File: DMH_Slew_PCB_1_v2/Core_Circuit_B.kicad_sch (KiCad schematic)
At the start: 52 parts, among them J6 TS_Jack_6.35mm_Sw, J60 Conn_01x08_PinHeader, J61 Conn_01x08_PinHeader, J7 TS_Jack_6.35mm_Sw, J8 TS_Jack_6.35mm_Sw, Q10 BC558, Q7 BC548, Q8 BC548, Q9 BC558, SW4 SW_DPDT_3way, SW5 SW_DPDT, SW6 SPDT_OnOffOn, U3 TL074, U4 TL074

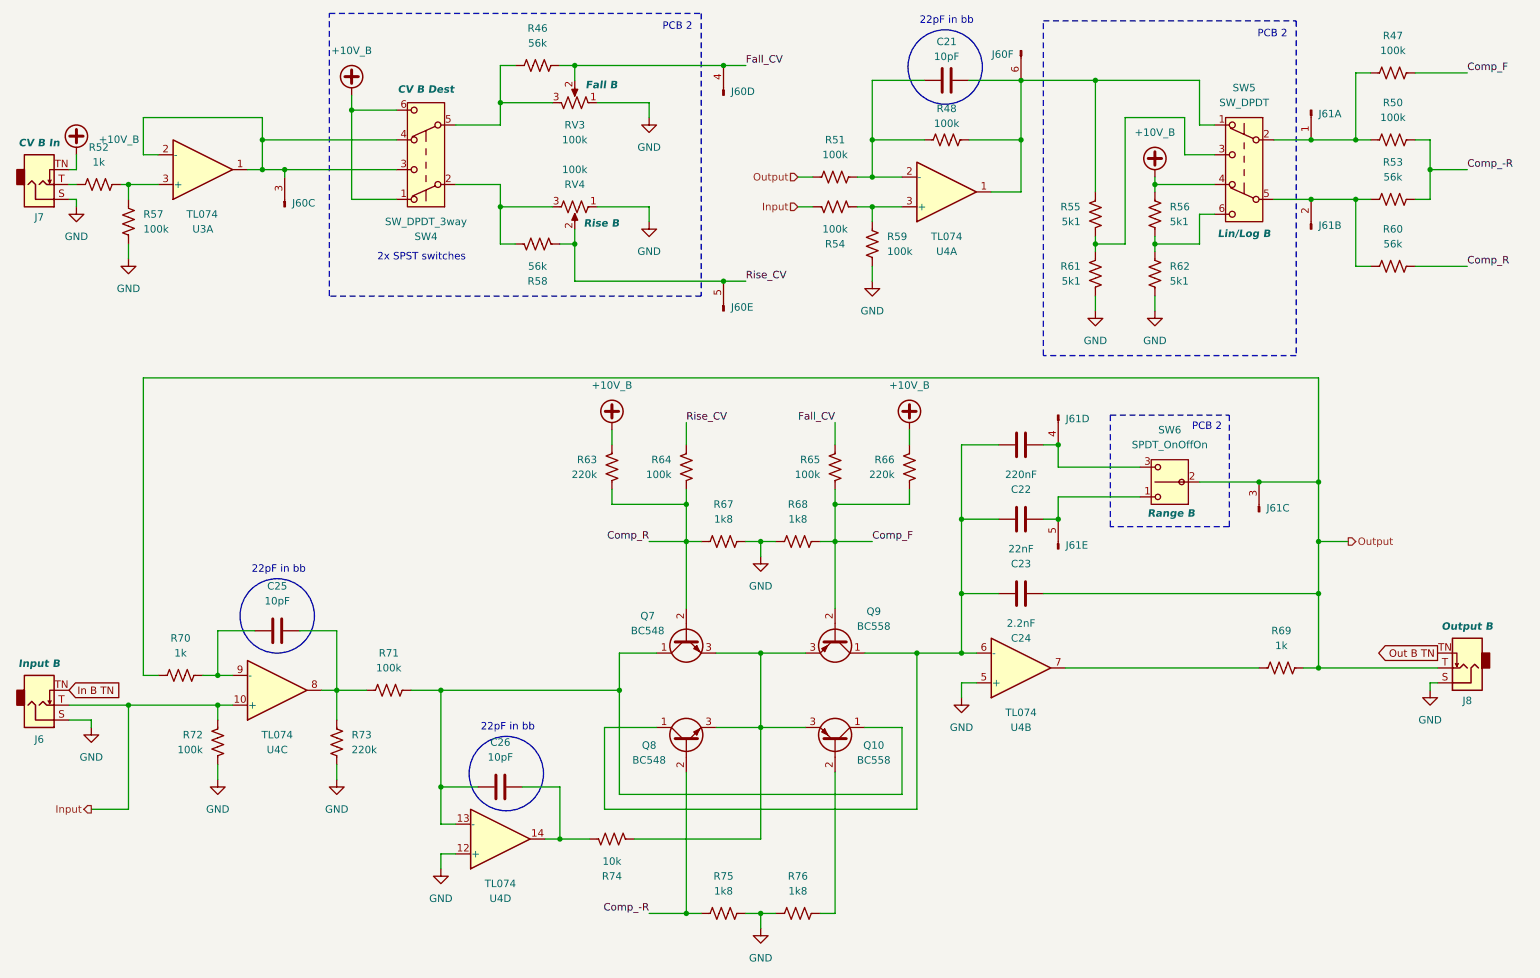
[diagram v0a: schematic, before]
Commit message: PCB 2 component placement done
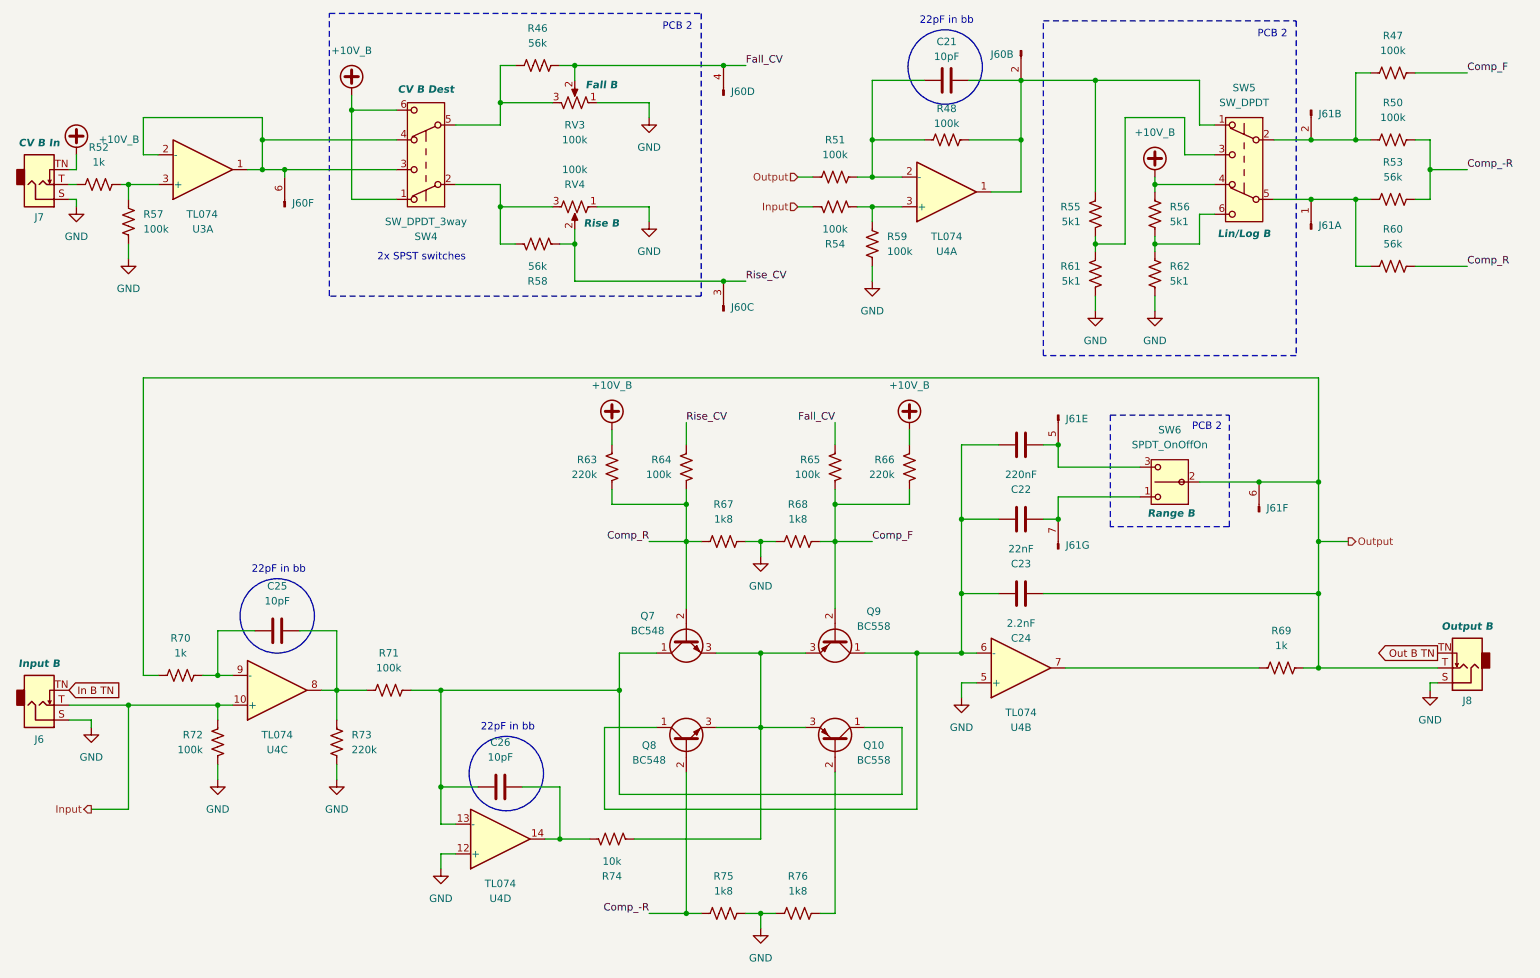
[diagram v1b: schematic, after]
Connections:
- net Output: now also J61.6 (Pin_6); no longer J61.3 (Pin_3)
- net Rise_CV: now also J60.3 (Pin_3); no longer J60.5 (Pin_5)
- net at C21.2, R48.1, R55.1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: now also J60.2 (Pin_2); no longer J60.6 (Pin_6)
- net at C22.2, SW6.3 (C): now also J61.5 (Pin_5); no longer J61.4 (Pin_4)
- net at R53.2, R60.2, SW5.5 (B): now also J61.1 (Pin_1); no longer J61.2 (Pin_2)
- net at SW4.3 (C), SW4.4 (A), U3.1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: now also J60.6 (Pin_6); no longer J60.3 (Pin_3)
- net at R47.2, R50.2, SW5.2 (B): now also J61.2 (Pin_2); no longer J61.1 (Pin_1)
- net at C23.2, SW6.1 (A): now also J61.7 (Pin_7); no longer J61.5 (Pin_5)
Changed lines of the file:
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@@
 		(at 190.5 30.48 90)
 		(mirror x)
-		(unit 6)
+		(unit 2)
 		(exclude_from_sim no)
 		(in_bom yes)
@@
 				(path "/58f4306d-5387-4983-bb08-41a2313fd315/77d402a4-d1d6-4e9c-af86-3ca5793147b8"
 					(reference "J60")
-					(unit 6)
+					(unit 2)
 				)
 			)
@@
 		(lib_id "SynthStuff:Conn_01x08_PinHeader")
 		(at 240.03 60.96 90)
-		(unit 2)
+		(unit 1)
 		(exclude_from_sim no)
 		(in_bom yes)
@@
 				(path "/58f4306d-5387-4983-bb08-41a2313fd315/77d402a4-d1d6-4e9c-af86-3ca5793147b8"
 					(reference "J61")
-					(unit 2)
+					(unit 1)
 				)
 			)
@@
 		(lib_id "SynthStuff:Conn_01x08_PinHeader")
 		(at 231.14 109.22 90)
-		(unit 3)
+		(unit 6)
 		(exclude_from_sim no)
 		(in_bom yes)
@@
 				(path "/58f4306d-5387-4983-bb08-41a2313fd315/77d402a4-d1d6-4e9c-af86-3ca5793147b8"
 					(reference "J61")
-					(unit 3)
+					(unit 6)
 				)
 			)
@@
 		(lib_id "SynthStuff:Conn_01x08_PinHeader")
 		(at 196.85 115.57 90)
-		(unit 5)
+		(unit 7)
 		(exclude_from_sim no)
 		(in_bom yes)
@@
 				(path "/58f4306d-5387-4983-bb08-41a2313fd315/77d402a4-d1d6-4e9c-af86-3ca5793147b8"
 					(reference "J61")
-					(unit 5)
+					(unit 7)
 				)
 			)
@@
 		(lib_id "SynthStuff:Conn_01x08_PinHeader")
 		(at 64.77 57.15 90)
-		(unit 3)
+		(unit 6)
 		(exclude_from_sim no)
 		(in_bom yes)
@@
 				(path "/58f4306d-5387-4983-bb08-41a2313fd315/77d402a4-d1d6-4e9c-af86-3ca5793147b8"
 					(reference "J60")
-					(unit 3)
+					(unit 6)
 				)
 			)
@@
 		(lib_id "SynthStuff:Conn_01x08_PinHeader")
 		(at 196.85 92.71 270)
-		(unit 4)
+		(unit 5)
 		(exclude_from_sim no)
 		(in_bom yes)
@@
 				(path "/58f4306d-5387-4983-bb08-41a2313fd315/77d402a4-d1d6-4e9c-af86-3ca5793147b8"
 					(reference "J61")
-					(unit 4)
+					(unit 5)
 				)
 			)
@@
 		(lib_id "SynthStuff:Conn_01x08_PinHeader")
 		(at 240.03 40.64 270)
-		(unit 1)
+		(unit 2)
 		(exclude_from_sim no)
 		(in_bom yes)
@@
 				(path "/58f4306d-5387-4983-bb08-41a2313fd315/77d402a4-d1d6-4e9c-af86-3ca5793147b8"
 					(reference "J61")
-					(unit 1)
+					(unit 2)
 				)
 			)
@@
 		(lib_id "SynthStuff:Conn_01x08_PinHeader")
 		(at 139.7 74.93 90)
-		(unit 5)
+		(unit 3)
 		(exclude_from_sim no)
 		(in_bom yes)
@@
 				(path "/58f4306d-5387-4983-bb08-41a2313fd315/77d402a4-d1d6-4e9c-af86-3ca5793147b8"
 					(reference "J60")
-					(unit 5)
+					(unit 3)
 				)
 			)

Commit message: PCB 1 component placement ongoing
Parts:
- Q10, Q8: footprint Package_TO_SOT_THT:TO-92_Inline -> Package_TO_SOT_THT:TO-92L_Inline_Wide
- U3: footprint Package_DIP:DIP-16_W7.62mm_Socket -> Package_DIP:DIP-14_W7.62mm_Socket
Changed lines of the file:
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@@
 			)
 		)
-		(property "Footprint" "Package_TO_SOT_THT:TO-92_Inline"
+		(property "Footprint" "Package_TO_SOT_THT:TO-92L_Inline_Wide"
 			(at 156.845 143.51 0)
 			(effects
@@
 			)
 		)
-		(property "Footprint" "Package_TO_SOT_THT:TO-92_Inline"
+		(property "Footprint" "Package_TO_SOT_THT:TO-92L_Inline_Wide"
 			(at 135.255 143.51 0)
 			(effects
@@
 			)
 		)
-		(property "Footprint" "Package_DIP:DIP-16_W7.62mm_Socket"
+		(property "Footprint" "Package_DIP:DIP-14_W7.62mm_Socket"
 			(at 49.53 53.34 0)
 			(effects

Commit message: Updated Log circuit
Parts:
- removed R55, R56, R61, R62: 5k1, Resistor_THT:R_Axial_DIN0207_L6.3mm_D2.5mm_P7.62mm_Horizontal, symbol Device:R_US
- R53, R60: value 56k -> 100k
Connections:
- net GND: now also SW5.3 (C), SW5.6 (C)
